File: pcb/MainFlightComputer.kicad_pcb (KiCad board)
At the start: 4 copper layers, 60 x 50 mm, 74 parts, among them J1 614105150721, J3 0472192001, J4 Pinout, J5 Debug, SW1 B3U-1000P, SW2 B3U-1000P, U1 STM32H533VET6, U2 MCP2221A-I/ST, U3 AP2112K-3.3

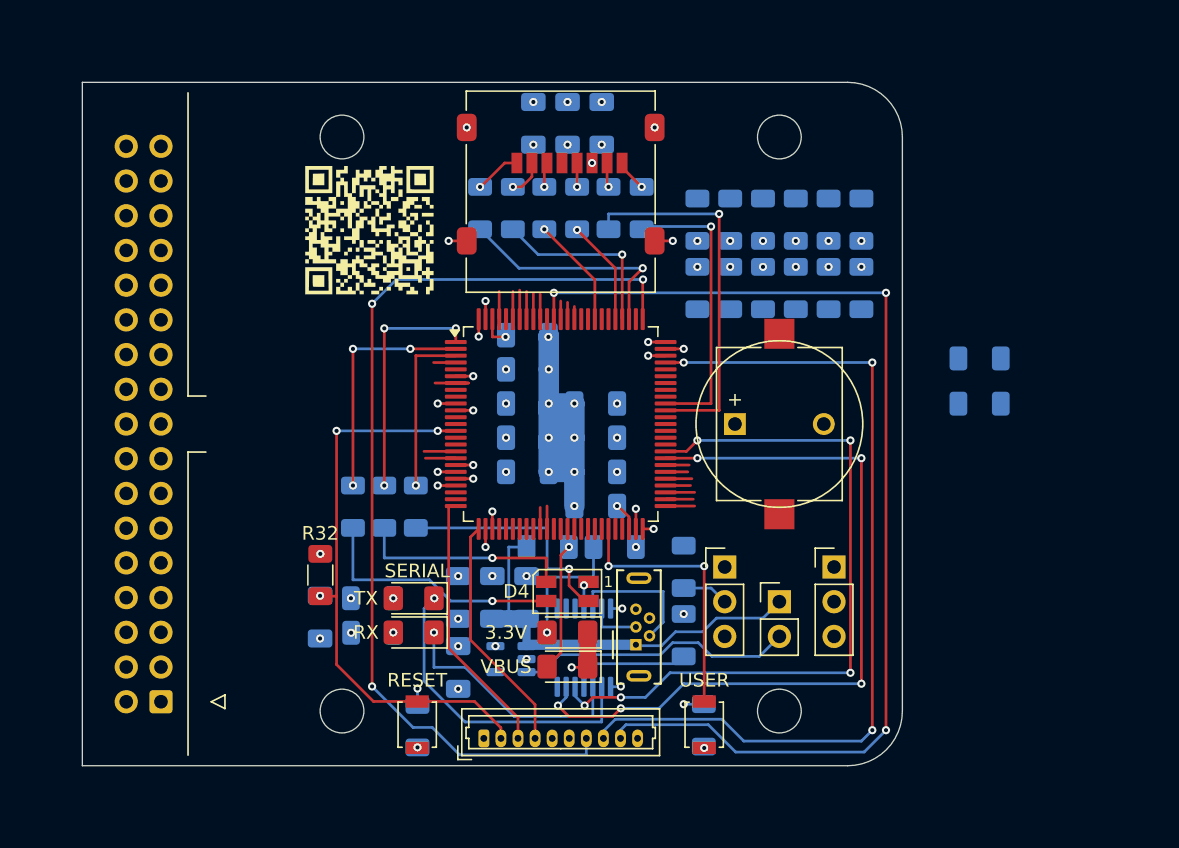
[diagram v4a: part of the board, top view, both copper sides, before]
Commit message: Centered the edge-cut.
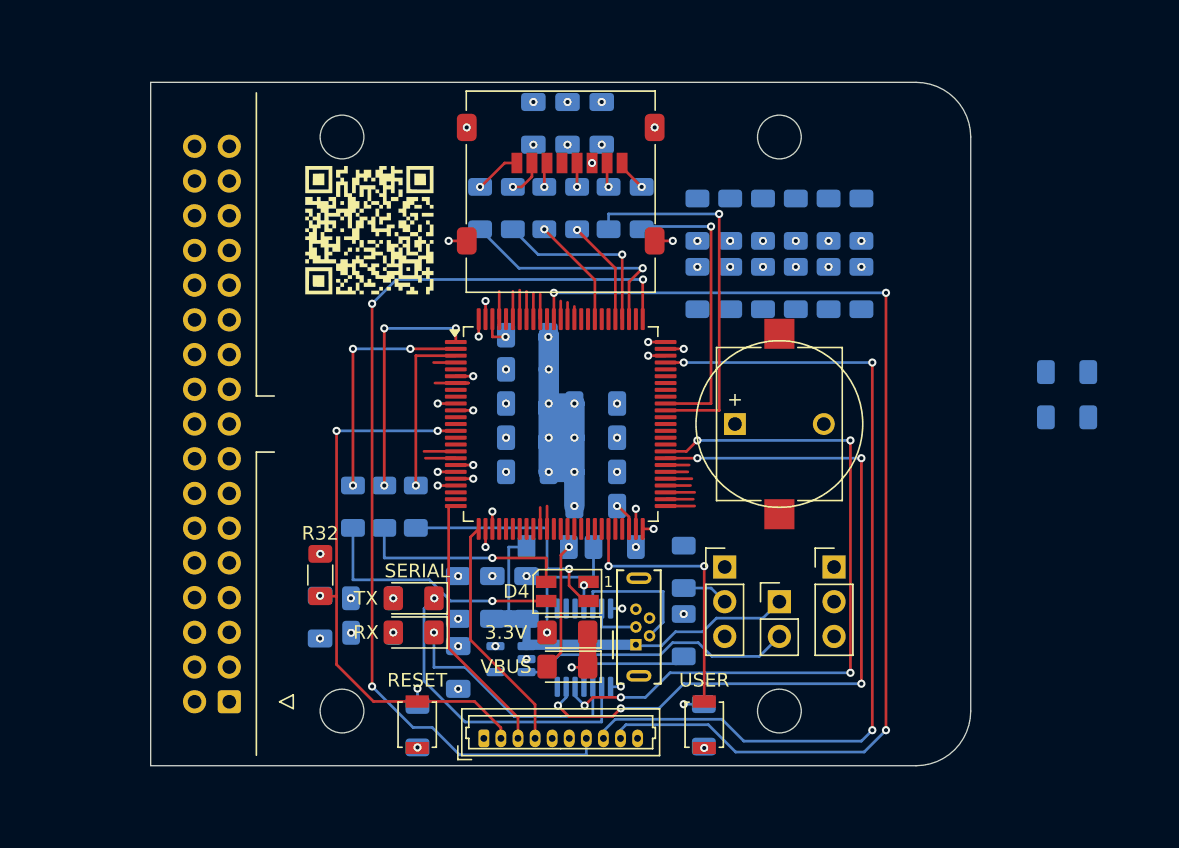
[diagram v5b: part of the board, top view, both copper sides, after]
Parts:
- moved R10 6.48 mm to (187.1, 99.5)
- moved R9 6.48 mm to (187.1, 96.2)
- moved J4 5.00 mm to (125.8, 120.3)
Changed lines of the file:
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@@
 	)
 	(footprint "pcb:IDC-Header_2x17_P2.54mm_Vertical"
+		(locked yes)
 		(layer "F.Cu")
-		(at 120.7525 120.32 180)
+		(at 125.7525 120.32 180)
 		(descr "Through hole IDC box header, 2x17, 2.54mm pitch, DIN 41651 / IEC 60603-13, double rows, https://docs.google.com/spreadsheets/d/16SsEcesNF15N3Lb4niX7dcUr-NY5_MFPQhobNuNppn4/edit#gid=0")
 		(tags "Through hole vertical IDC box header THT 2x17 2.54mm double row")
@@
 			(opacity 0.9000)
 			(offset
-				(xyz -10 24 31)
+				(xyz 0 24 31)
 			)
 			(scale
@@
 	(footprint "Resistor_SMD:R_1206_3216Metric_Pad1.30x1.75mm_HandSolder"
 		(layer "B.Cu")
-		(at 180.65 98.51 180)
+		(at 187.05 99.51 180)
 		(descr "Resistor SMD 1206 (3216 Metric), square (rectangular) end terminal, IPC-7351 nominal with elongated pad for handsoldering. (Body size source: IPC-SM-782 page 72, https://www.pcb-3d.com/wordpress/wp-content/uploads/ipc-sm-782a_amendment_1_and_2.pdf), generated with kicad-footprint-generator")
 		(tags "resistor handsolder")
@@
 	(footprint "Resistor_SMD:R_1206_3216Metric_Pad1.30x1.75mm_HandSolder"
 		(layer "B.Cu")
-		(at 180.65 95.2 180)
+		(at 187.05 96.2 180)
 		(descr "Resistor SMD 1206 (3216 Metric), square (rectangular) end terminal, IPC-7351 nominal with elongated pad for handsoldering. (Body size source: IPC-SM-782 page 72, https://www.pcb-3d.com/wordpress/wp-content/uploads/ipc-sm-782a_amendment_1_and_2.pdf), generated with kicad-footprint-generator")
 		(tags "resistor handsolder")
@@
 	)
 	(gr_line
-		(start 171 125)
-		(end 115 125)
+		(start 176 125)
+		(end 120 125)
 		(stroke
 			(width 0.05)
 			(type default)
 		)
+		(locked yes)
 		(layer "Edge.Cuts")
 	)
 	(gr_arc
-		(start 171 75)
-		(mid 173.828427 76.171573)
-		(end 175 79)
+		(start 176 75)
+		(mid 178.828427 76.171573)
+		(end 180 79)
 		(stroke
 			(width 0.05)
@@
 	)
 	(gr_line
-		(start 115 75)
-		(end 171 75)
+		(start 120 75)
+		(end 176 75)
 		(stroke
 			(width 0.05)
 			(type default)
 		)
+		(locked yes)
 		(layer "Edge.Cuts")
 	)
 	(gr_line
-		(start 175 79)
-		(end 175 121)
+		(start 180 79)
+		(end 180 121)
 		(stroke
 			(width 0.05)
@@
 	)
 	(gr_arc
-		(start 175 121)
-		(mid 173.828427 123.828427)
-		(end 171 125)
+		(start 180 121)
+		(mid 178.828427 123.828427)
+		(end 176 125)
 		(stroke
 			(width 0.05)
@@
 	)
 	(gr_line
-		(start 115 125)
-		(end 115 75)
+		(start 120 125)
+		(end 120 75)
 		(stroke
 			(width 0.05)
 			(type default)
 		)
+		(locked yes)
 		(layer "Edge.Cuts")
 	)

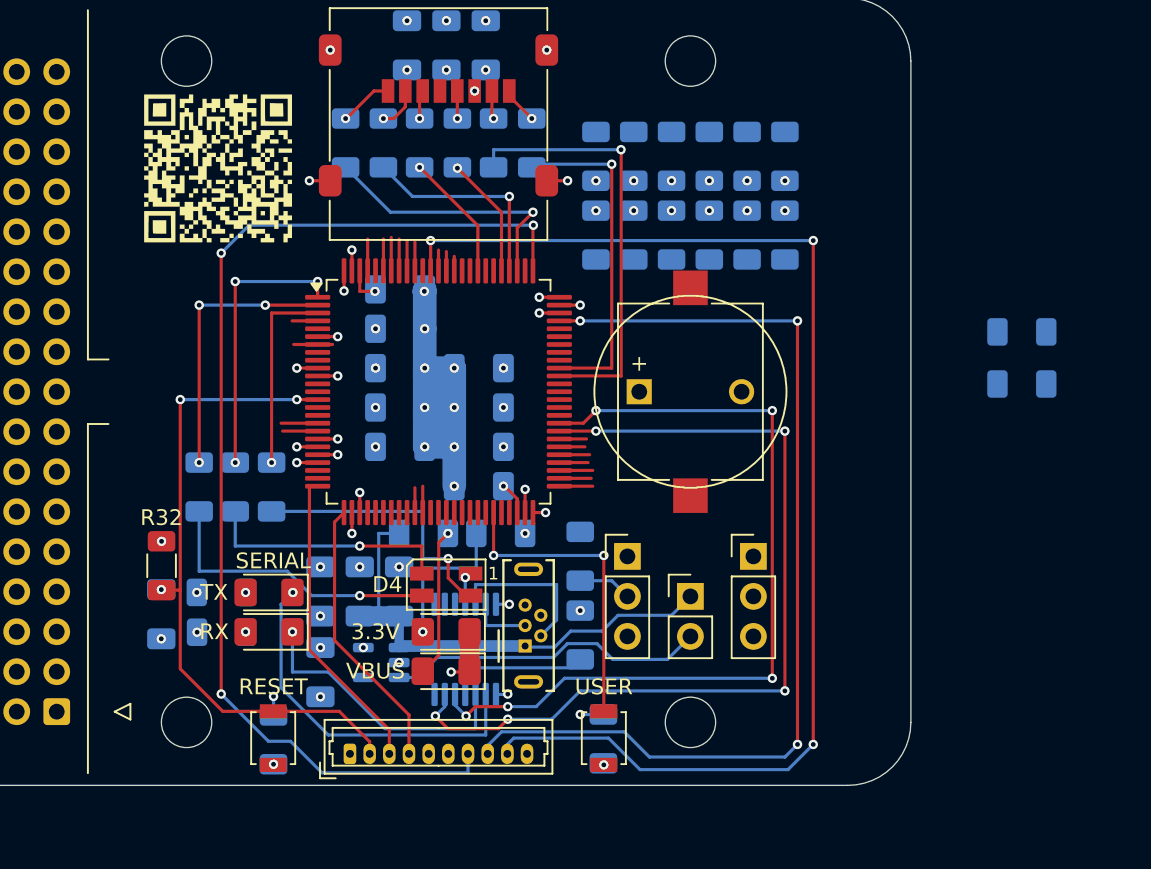
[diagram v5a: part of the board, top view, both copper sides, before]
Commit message: Footprints in place.
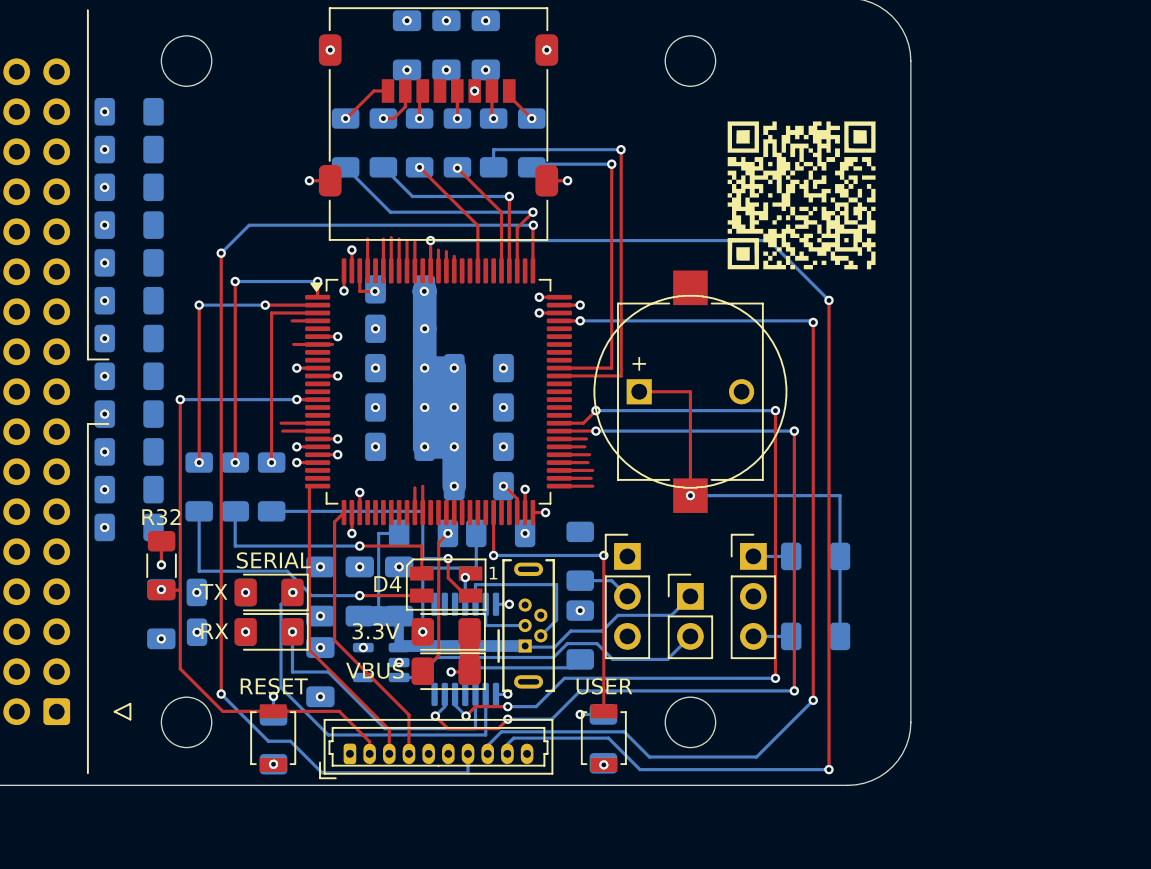
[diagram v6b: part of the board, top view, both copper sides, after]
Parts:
- moved R24 47.9 mm to (130.4, 108.6), turned to 180 degrees
- moved R23 44.6 mm to (130.4, 106.2), turned to 180 degrees
- moved R26 42.4 mm to (130.4, 82.2), turned to 180 degrees
- moved R21 41.4 mm to (130.4, 103.8), turned to 180 degrees
- moved R27 39.6 mm to (130.4, 84.6), turned to 180 degrees
- moved R20 38.1 mm to (130.4, 101.4), turned to 180 degrees
- moved G*** 37.1 mm to (173.1, 87.5)
- moved R28 37.0 mm to (130.4, 87.0), turned to 180 degrees
- moved R25 35.0 mm to (130.4, 99.0), turned to 180 degrees
- moved R29 34.5 mm to (130.4, 89.4), turned to 180 degrees
- moved R30 32.1 mm to (130.4, 91.8), turned to 180 degrees
- moved R22 31.8 mm to (130.4, 96.6), turned to 180 degrees
- moved R31 29.9 mm to (130.4, 94.2), turned to 180 degrees
- moved R10 20.7 mm to (173.9, 115.5), turned to 0 degrees
- moved R9 19.4 mm to (174.0, 110.5), turned to 0 degrees
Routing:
- net Net-(BZ1-+): track 0.00 -> 28.3 mm, vias 0 -> 1
- net Net-(JP3-A): track 0.00 -> 2.40 mm
- net Net-(JP3-B): track 0.00 -> 2.40 mm
- net +3.3V: track 13.5 -> 15.0 mm
- net serial_rx: track 56.0 -> 57.2 mm
- net swo: track 79.9 -> 80.6 mm

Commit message: Finished routing main flight computer.
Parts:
- moved R21 14.4 mm to (130.4, 106.2)
- moved R2 12.0 mm to (130.4, 82.2)
- moved R14 9.62 mm to (130.4, 96.6)
- moved R12 9.58 mm to (130.4, 91.8)
- moved G*** 8.52 mm to (173.4, 79.0)
- moved R26 7.18 mm to (130.4, 108.6)
- moved R20 4.82 mm to (130.4, 103.8)
- moved R11 4.78 mm to (130.4, 89.4)
- moved R10 2.42 mm to (130.4, 87.0)
- moved R9 2.42 mm to (130.4, 84.6)
- moved R13 2.42 mm to (130.4, 94.2)
- moved R15 2.42 mm to (130.4, 101.4)
- moved R16 0.05 mm to (130.4, 99.0)
- renumbered BZ2 to BZ1, BZ1 to BZ2, C5 to C0, C6 to C1, C1 to C10, C17 to C11, C8 to C12, C7 to C13, C10 to C14, C11 to C15, C9 to C16, C4 to C2, C2 to C3, C3 to C4, C13 to C5, C14 to C6, C16 to C7, C15 to C8, C12 to C9, D4 to D1, D1 to D2, D2 to D3, D3 to D4, H4 to H1, H3 to H2, H1 to H3, H2 to H4, J3 to J1, J1 to J2, J4 to J3, J5 to J4, JP3 to JP2, JP2 to JP3, R32 to R1, R29 to R10, R27 to R11, R26 to R12, R22 to R13, R23 to R14, R21 to R15, R25 to R16, R13 to R17, R12 to R18, R11 to R19, R31 to R2, R24 to R20, R30 to R21, R9 to R22, R17 to R23, R14 to R24, R15 to R25, R20 to R26, R10 to R27, R19 to R28, R8 to R29, R7 to R30, R18 to R31, R16 to R32, R5 to R4, R6 to R5, R2 to R6, R1 to R7, R4 to R8, R28 to R9
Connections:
- net /SD_CLK renamed /SD_CONNECTOR_CLK
- net /SD_CMD renamed /SD_CONNECTOR_CMD
- net /SD_DAT0 renamed /SD_CONNECTOR_DAT0
- net /SD_DAT1 renamed /SD_CONNECTOR_DAT1
- net /SD_DAT2 renamed /SD_CONNECTOR_DAT2
- net /SD_DAT3 renamed /SD_CONNECTOR_DAT3
- net Net-(BZ1-+) renamed /BUZZER_ANODE
- JP1 pad 1: GND -> +3.3V
- JP1 pad 3: +3.3V -> GND
- U1 pad 4: buzzer -> unconnected-(U1-PE5-Pad4)
- U1 pad 63: unconnected-(U1-PC6-Pad63) -> buzzer
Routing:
- net uart_rx_B: track 1.62 -> 110.6 mm, vias 0 -> 4
- net uart_tx_B: track 1.92 -> 109.7 mm, vias 0 -> 2
- net uart_rx_A: track 1.82 -> 86.0 mm, vias 0 -> 4
- net spi_nss_A: track 2.12 -> 82.4 mm, vias 0 -> 5
- net /BOOT0: track 2.12 -> 81.0 mm, vias 0 -> 3
- net uart_tx_A: track 2.12 -> 67.3 mm, vias 0 -> 2
- net spi_mosi_A: track 2.22 -> 54.1 mm, vias 0 -> 4
- net general_purpose_B: track 0.00 -> 49.7 mm, vias 0 -> 4
- net spi_nss_B: track 2.03 -> 46.7 mm, vias 0 -> 2
- net spi_mosi_B: track 1.83 -> 45.4 mm, vias 0 -> 3
- net spi_clock_A: track 0.00 -> 41.9 mm, vias 0 -> 1
- net spi_ready_A: track 0.92 -> 40.6 mm, vias 0 -> 3
- net general_purpose_A: track 0.00 -> 38.9 mm, vias 0 -> 3
- net i2c_clock_B: track 1.23 -> 36.3 mm, vias 0 -> 2
- net spi_ready_B: track 2.03 -> 35.6 mm, vias 0 -> 4
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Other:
- board size 60 x 50 mm -> 60 x 60 mm
- board text added: "0"
- board text added: "1"
- board text added: "BOOT0"
- board text added: "LOUD"
- board text added: "QUIET"

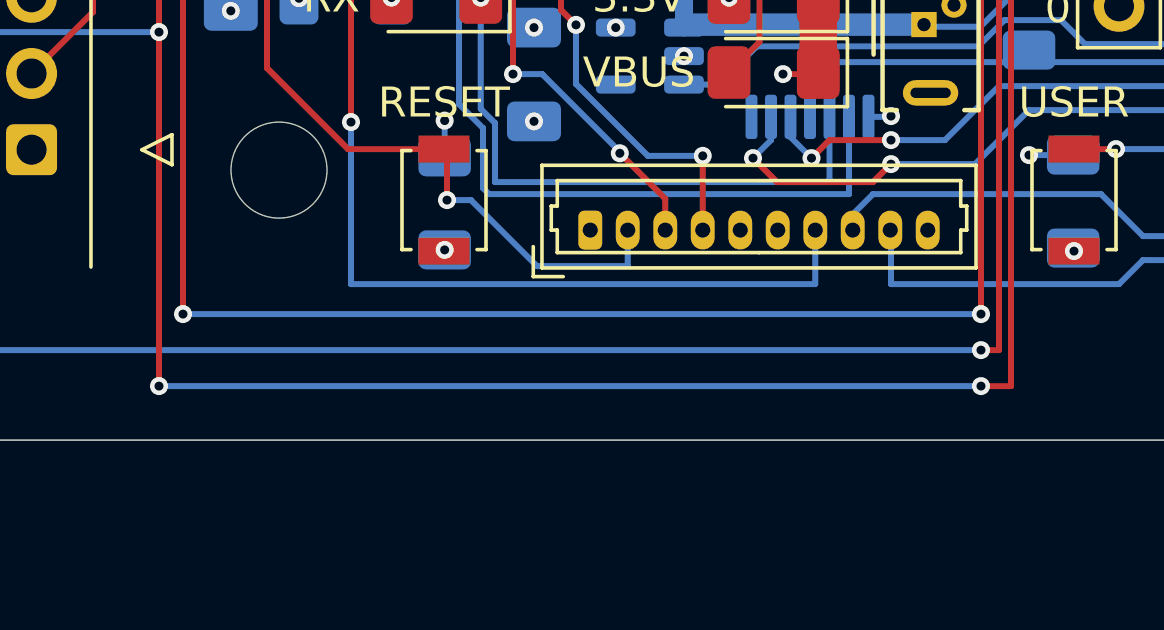
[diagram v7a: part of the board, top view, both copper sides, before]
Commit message: Added test pads for debug connector.
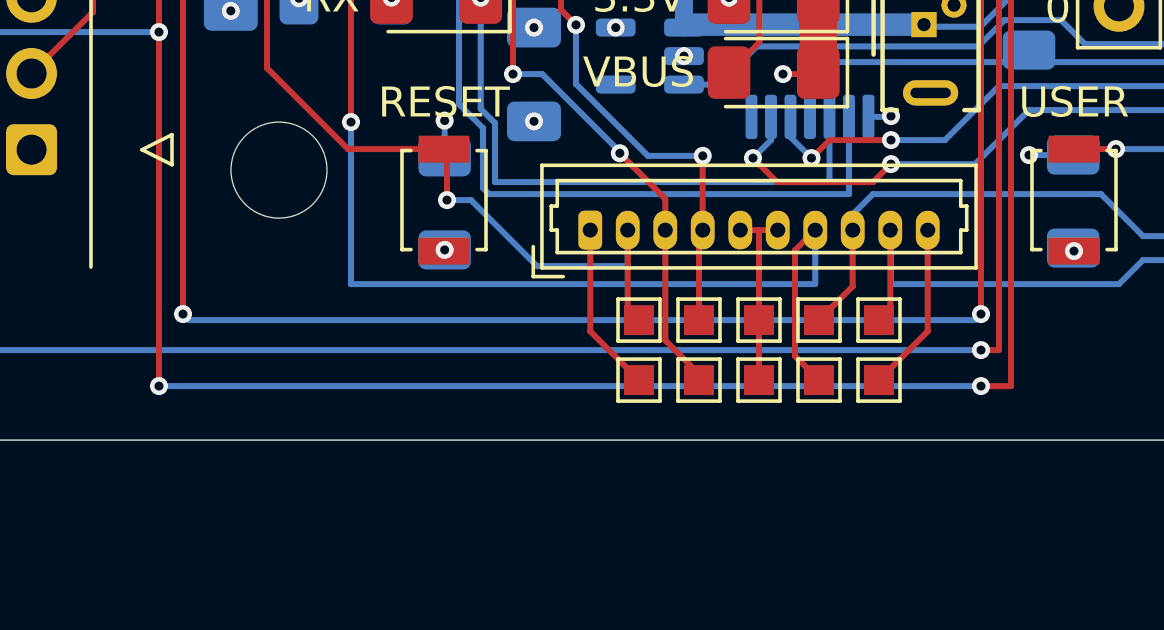
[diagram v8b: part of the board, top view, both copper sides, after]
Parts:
- added TP1: TestPoint, TestPoint:TestPoint_Pad_1.0x1.0mm, F.Cu at (146.0, 126.0)
- added TP10: TestPoint, TestPoint:TestPoint_Pad_1.0x1.0mm, F.Cu at (154.0, 128.0)
- added TP2: TestPoint, TestPoint:TestPoint_Pad_1.0x1.0mm, F.Cu at (148.0, 126.0)
- added TP3: TestPoint, TestPoint:TestPoint_Pad_1.0x1.0mm, F.Cu at (152.0, 126.0)
- added TP4: TestPoint, TestPoint:TestPoint_Pad_1.0x1.0mm, F.Cu at (150.0, 126.0)
- added TP5: TestPoint, TestPoint:TestPoint_Pad_1.0x1.0mm, F.Cu at (154.0, 126.0)
- added TP6: TestPoint, TestPoint:TestPoint_Pad_1.0x1.0mm, F.Cu at (146.0, 128.0)
- added TP7: TestPoint, TestPoint:TestPoint_Pad_1.0x1.0mm, F.Cu at (152.0, 128.0)
- added TP8: TestPoint, TestPoint:TestPoint_Pad_1.0x1.0mm, F.Cu at (150.0, 128.0)
- added TP9: TestPoint, TestPoint:TestPoint_Pad_1.0x1.0mm, F.Cu at (148.0, 128.0)
- renumbered BZ2 to BZ1, BZ1 to BZ2, C2 to C1, C9 to C10, C13 to C12, C12 to C13, C1 to C2, C6 to C5, C5 to C6, C8 to C7, C7 to C8, C10 to C9, D3 to D2, D2 to D3, R16 to R15, R15 to R16, R19 to R18, R18 to R19, R30 to R29, R4 to R3, R29 to R30, R3 to R4, R8 to R7, R7 to R8
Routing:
- net GND: track 52.3 -> 64.2 mm
- net +3.3V: track 15.6 -> 21.3 mm
- net swclk: track 102.8 -> 108.4 mm
- net stlink_tx: track 20.2 -> 25.7 mm
- net swdio: track 65.9 -> 69.4 mm
- net RESET: track 44.5 -> 47.6 mm
- net swo: track 85.8 -> 89.0 mm
- net stlink_rx: track 18.6 -> 21.7 mm
